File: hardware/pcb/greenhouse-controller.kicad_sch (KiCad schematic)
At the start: 66 parts, among them J1 Motor 2, J10 ALARM contact, J2 Screw_Terminal_01x02, J3 I2C Display, J4 Keypad, J5 MODBUS RS485, J6 Motor 3, J7 Motor 1, J8 SD-Card-slot, Q1 2N7000, Q2 2N7000, Q3 2N7000, Q4 2N7000, Q5 2N7000, Q6 2N7000, U1 Wemos_S3_ESP32-S3, U2 BUCK-30V-5V, U3 SIT65HVD08P, U4 DS1307Z+, Y1 32.768 kHz

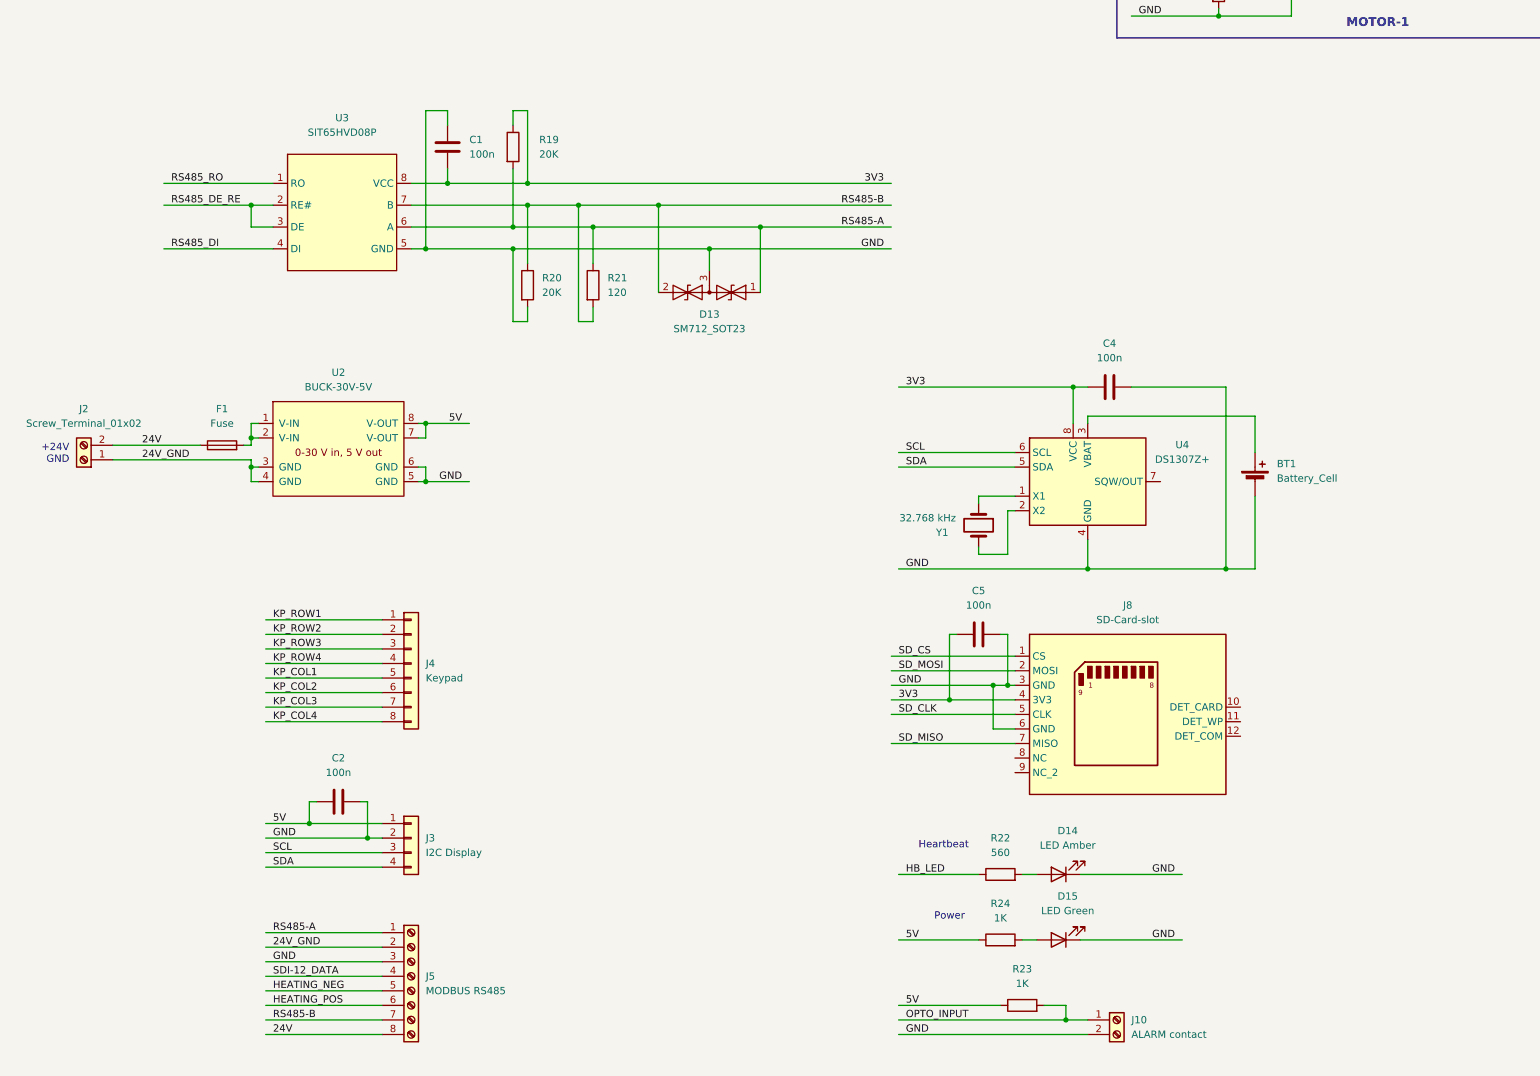
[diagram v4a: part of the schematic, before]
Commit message: Initiele componentplaatsing PCB
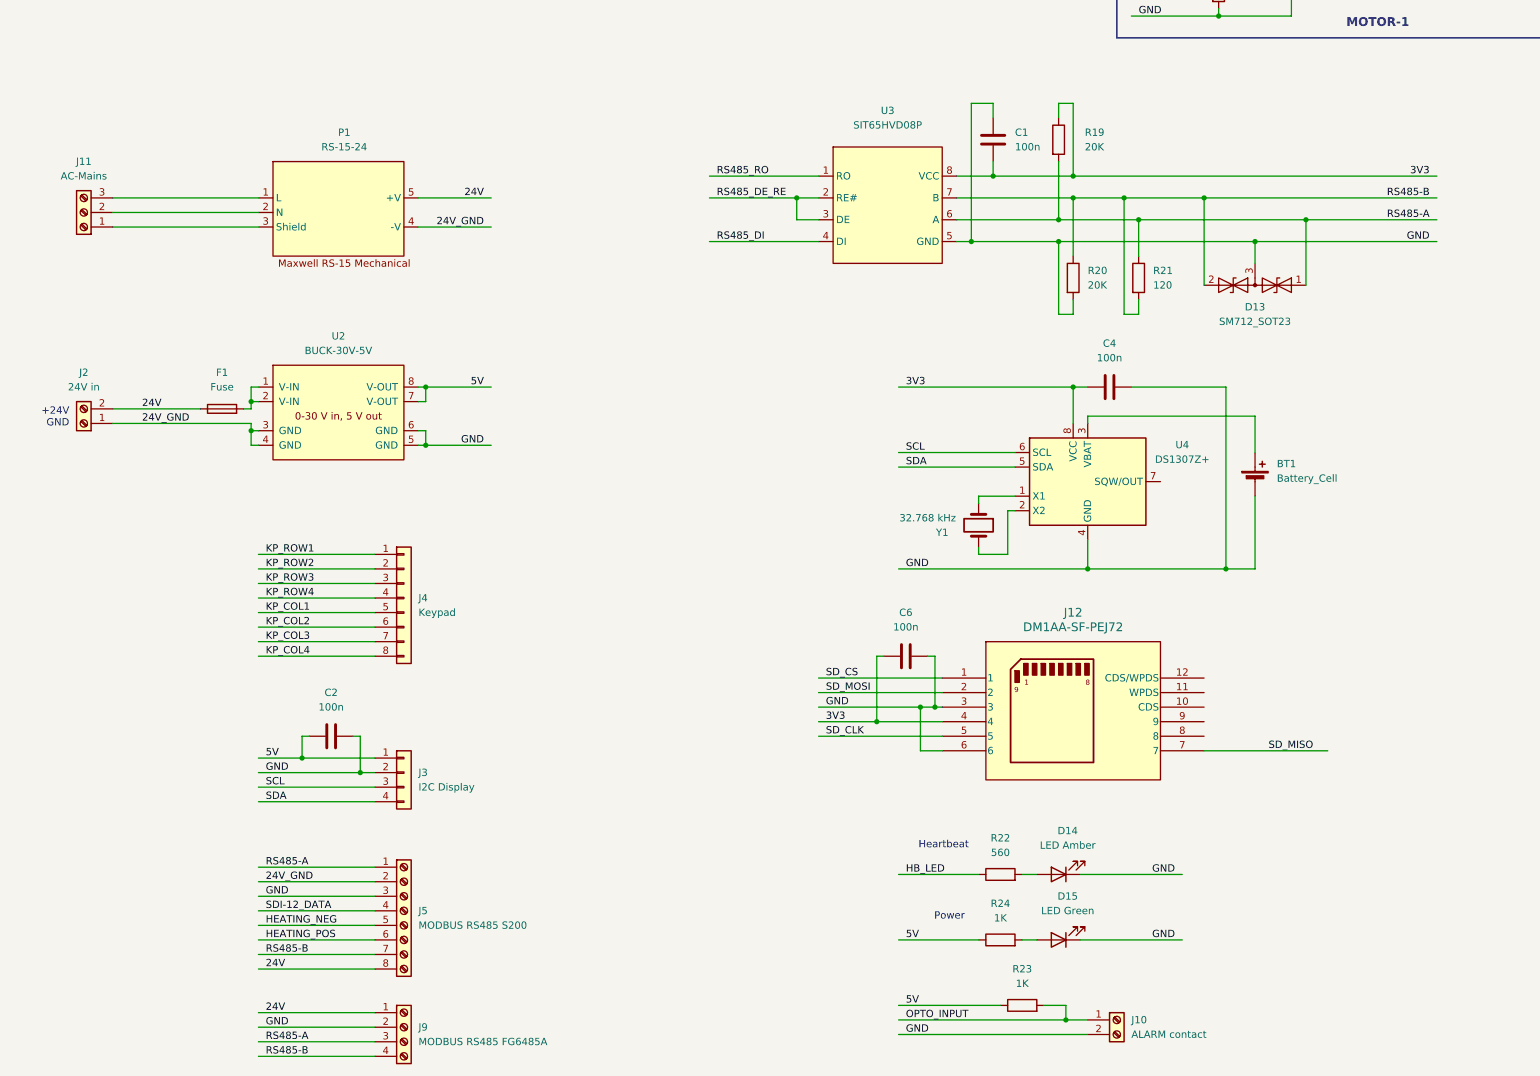
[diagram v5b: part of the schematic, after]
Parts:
- removed C5: 100n, Capacitor_SMD:C_1206_3216Metric_Pad1.33x1.80mm_HandSolder, symbol Device:C
- removed J8: SD-Card-slot, symbol my-KiCad-library:SD-Socket
- added C6: 100n, Capacitor_SMD:C_1206_3216Metric_Pad1.33x1.80mm_HandSolder, symbol Device:C
- added J11: AC-Mains, TerminalBlock_Phoenix:TerminalBlock_Phoenix_MKDS-1,5-3_1x03_P5.00mm_Horizontal, symbol Connector:Screw_Terminal_01x03
- added J12: DM1AA-SF-PEJ72, my-KiCad-library:DM1AA-SF-PEJ72_HIR, symbol my-KiCad-library:DM1AA-SF-PEJ72
- added J9: MODBUS RS485 FG6485A, TerminalBlock_Phoenix:TerminalBlock_Phoenix_MKDS-1,5-4_1x04_P5.00mm_Horizontal, symbol Connector:Screw_Terminal_01x04
- added P1: RS-15-24, my-KiCad-library:Meanwell RS-15 Mechanical, symbol my-KiCad-library:Maxwell RS15 Mechanical
- BT1: footprint (none) -> Battery:BatteryHolder_MYOUNG_BS-07-A1BJ001_CR2032
- J1, J6, J7: footprint (none) -> TerminalBlock_Phoenix:TerminalBlock_Phoenix_MKDS-1,5-4_1x04_P5.00mm_Horizontal
- J10: footprint (none) -> TerminalBlock_Phoenix:TerminalBlock_Phoenix_MKDS-1,5-2_1x02_P5.00mm_Horizontal
- J2: value Screw_Terminal_01x02 -> 24V in; footprint (none) -> TerminalBlock_Phoenix:TerminalBlock_Phoenix_MKDS-1,5-2_1x02_P5.00mm_Horizontal
- J3: footprint (none) -> Connector_PinHeader_2.54mm:PinHeader_1x04_P2.54mm_Vertical
- J4: footprint (none) -> Connector_PinHeader_2.54mm:PinHeader_1x08_P2.54mm_Vertical
- J5: value MODBUS RS485 -> MODBUS RS485 S200; footprint (none) -> TerminalBlock_Phoenix:TerminalBlock_Phoenix_MKDS-1,5-8_1x08_P5.00mm_Horizontal
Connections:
- net 24V: now also J9.1 (Pin_1), P1.5 (+V)
- net 24V_GND: now also P1.4 (-V)
- net 3V3: now also C6.1, J12.4
- net GND: now also C6.2, J12.3, J12.6, J9.2 (Pin_2)
- net RS485-A: now also J9.3 (Pin_3)
- net RS485-B: now also J9.4 (Pin_4)
- net SD_CLK: now also J12.5
- net SD_CS: now also J12.1
- net SD_MISO: now also J12.7
- net SD_MOSI: now also J12.2
- new net: J11.1 (Pin_1), P1.3 (Shield)
- new net: J11.2 (Pin_2), P1.2 (N)
- new net: J11.3 (Pin_3), P1.1 (L)
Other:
- moved on the sheet: C1, C2, D13, F1, J2, J3, J4, J5, R19, R20, R21, U2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

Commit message: Some corrections
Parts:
- added M1: LCD1602 I2C Module mechanical, my-KiCad-library:LCD1602 I2C Module mechanical, symbol my-KiCad-library:LCD1602_I2C_Module_mechanical
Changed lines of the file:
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@@
+	)
+	(symbol
+		(lib_id "my-KiCad-library:LCD1602_I2C_Module_mechanical")
+		(at 363.22 242.57 0)
+		(unit 1)
+		(exclude_from_sim no)
+		(in_bom yes)
+		(on_board yes)
+		(dnp no)
+		(fields_autoplaced yes)
+		(property "Reference" "M1"
+			(at 372.11 245.7449 0)
+			(effects
+				(font
+					(size 1.27 1.27)
+				)
+				(justify left)
+			)
+		)
+		(property "Value" "LCD1602 I2C Module mechanical"
+			(at 372.11 248.2849 0)
+			(effects
+				(font
+					(size 1.27 1.27)
+				)
+				(justify left)
+			)
+		)
+		(property "Footprint" "my-KiCad-library:LCD1602 I2C Module mechanical"
+			(at 363.22 242.57 0)
+			(effects
+				(font
+					(size 1.27 1.27)
+				)
+				(hide yes)
+			)
+		)
+		(property "Datasheet" ""
+			(at 363.22 242.57 0)
+			(effects
+				(font
+					(size 1.27 1.27)
+				)
+				(hide yes)
+			)
+		)
+		(property "Description" ""
+			(at 363.22 242.57 0)
+			(effects
+				(font
+					(size 1.27 1.27)
+				)
+				(hide yes)
+			)
+		)
+		(instances
+			(project ""
+				(path "/2be5eb1b-bfdc-4766-9909-5178f7452cd9"
+					(reference "M1")
+					(unit 1)
+				)
+			)
+		)
 	)
 	(symbol

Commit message: ìntermediate update of PCB design
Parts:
- removed F1: Fuse, symbol Device:Fuse
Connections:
- net 24V: now also U2.1 (V-IN), U2.2 (V-IN)
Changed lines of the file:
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@@
 	(wire
 		(pts
-			(xy 63.5 162.56) (xy 64.77 162.56)
-		)
-		(stroke
-			(width 0)
-			(type default)
-		)
-	)
-	(wire
-		(pts
 			(xy 326.39 138.43) (xy 339.09 138.43)
 		)
@@
 	(wire
 		(pts
-			(xy 40.64 162.56) (xy 55.88 162.56)
+			(xy 40.64 162.56) (xy 64.77 162.56)
 		)
 		(stroke
@@
 					(unit 1)
 				)
-			)
-		)
-	)
-	(symbol
-		(lib_id "Device:Fuse")
-		(at 59.69 162.56 90)
-		(unit 1)
-		(exclude_from_sim no)
-		(in_bom yes)
-		(on_board yes)
-		(dnp no)
-		(fields_autoplaced yes)
-		(property "Reference" "F1"
-			(at 59.69 156.21 90)
-			(effects
-				(font
-					(size 1.27 1.27)
-				)
-			)
-		)
-		(property "Value" "Fuse"
-			(at 59.69 158.75 90)
-			(effects
-				(font
-					(size 1.27 1.27)
-				)
-			)
-		)
-		(property "Footprint" ""
-			(at 59.69 164.338 90)
-			(effects
-				(font
-					(size 1.27 1.27)
-				)
-				(hide yes)
-			)
-		)
-		(property "Datasheet" "~"
-			(at 59.69 162.56 0)
-			(effects
-				(font
-					(size 1.27 1.27)
-				)
-				(hide yes)
-			)
-		)
-		(property "Description" "Fuse"
-			(at 59.69 162.56 0)
-			(effects
-				(font
-					(size 1.27 1.27)
-				)
-				(hide yes)
-			)
-		)
-		(pin "2"
-		)
-		(pin "1"
-		)
-		(instances
-			(project ""
-				(path "/2be5eb1b-bfdc-4766-9909-5178f7452cd9"
-					(reference "F1")
-					(unit 1)
-				)

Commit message: Intermediate update PCB
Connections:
- net 24V_GND is gone; now on net GND: J2.1 (Pin_1), J5.2 (Pin_2), P1.4 (-V), U2.3 (GND), U2.4 (GND)
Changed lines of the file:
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@@
 		)
 	)
-	(label "24V_GND"
+	(label "GND"
 		(at 67.31 245.11 0)
 		(effects
@@
 		)
 	)
-	(label "24V_GND"
+	(label "GND"
 		(at 45.72 165.1 0)
 		(effects
@@
 		)
 	)
-	(label "24V_GND"
+	(label "GND"
 		(at 105.41 130.81 180)
 		(effects
